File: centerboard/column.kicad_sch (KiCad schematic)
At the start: 5 parts

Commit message: centerboard messing around
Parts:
- added D1, D2, D3, D4: 1N4148W, Diode_SMD:D_SOD-123, symbol Diode:1N4148W
- added JC_LA: Conn_01x05_MountingPin, Connector_FFC-FPC:TE_84952-5_1x05-1MP_P1.0mm_Horizontal, symbol Connector_Generic_MountingPin:Conn_01x05_MountingPin
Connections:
- net COL: now also JC_LA.3 (Pin_3), JC_LA.3 (Pin_3); no longer JC_LA.5 (Pin_5)
- net at D3.2 (A): now also JC_LA.4 (Pin_4); no longer JC_LA.3 (Pin_3)
- net at D4.2 (A): now also JC_LA.5 (Pin_5); no longer JC_LA.4 (Pin_4)
- net ROW_1 renamed ROW_L4
- net ROW_2 renamed ROW_L3
- net ROW_3 renamed ROW_L2
- net ROW_4 renamed ROW_L1
- new net: D1.2 (A), JC_LA.1 (Pin_1)
- new net: D3.2 (A), JC_LA.4 (Pin_4)
- new net: D2.2 (A), JC_LA.2 (Pin_2)
- new net: D4.2 (A), JC_LA.5 (Pin_5)
- new net ROW_R1: D4.1 (K)
- new net ROW_R2: D3.1 (K)
- new net ROW_R3: D2.1 (K)
- new net ROW_R4: D1.1 (K)
- no-connect marks 0 -> 2

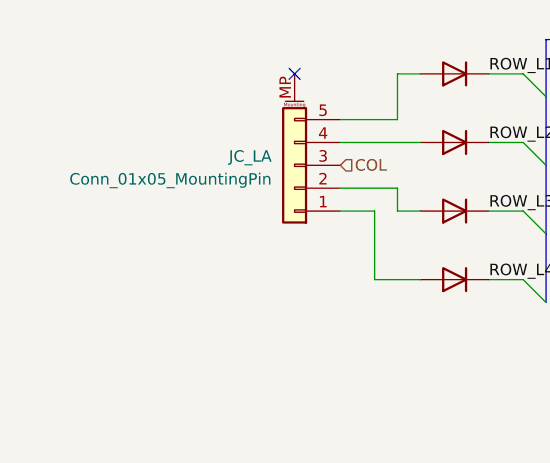
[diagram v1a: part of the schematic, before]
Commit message: Various tweaks. About to flip centerboard, not feeling too confident in the results there
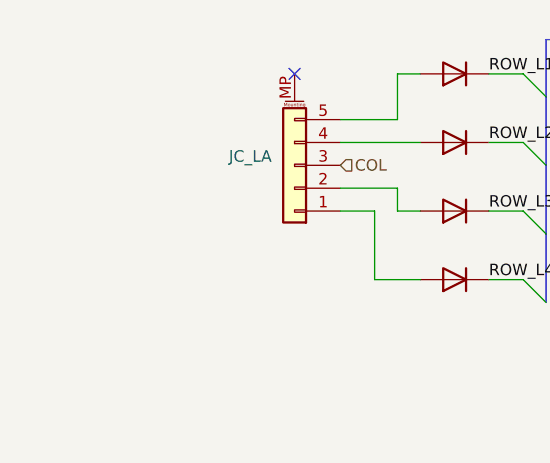
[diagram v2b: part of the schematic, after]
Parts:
- D1, D2, D3, D4: footprint Diode_SMD:D_SOD-123 -> Diode_SMD:D_0805_2012Metric
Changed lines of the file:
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@@
     )
     (property "Value" "Conn_01x05_MountingPin" (at 102.87 81.5594 0)
-      (effects (font (size 1.27 1.27)) (justify left))
+      (effects (font (size 1.27 1.27)) (justify left) hide)
     )
     (property "Footprint" "Connector_FFC-FPC:TE_84952-5_1x05-1MP_P1.0mm_Horizontal" (at 105.41 80.01 0)
@@
       (effects (font (size 1.27 1.27)) hide)
     )
-    (property "Footprint" "Diode_SMD:D_SOD-123" (at 207.01 111.125 0)
+    (property "Footprint" "Diode_SMD:D_0805_2012Metric" (at 207.01 111.125 0)
       (effects (font (size 1.27 1.27)) hide)
     )
@@
       (effects (font (size 1.27 1.27)) hide)
     )
-    (property "Footprint" "Diode_SMD:D_SOD-123" (at 123.19 88.265 0)
+    (property "Footprint" "Diode_SMD:D_0805_2012Metric" (at 123.19 88.265 0)
       (effects (font (size 1.27 1.27)) hide)
     )
@@
       (effects (font (size 1.27 1.27)) hide)
     )
-    (property "Footprint" "Diode_SMD:D_SOD-123" (at 207.01 95.885 0)
+    (property "Footprint" "Diode_SMD:D_0805_2012Metric" (at 207.01 95.885 0)
       (effects (font (size 1.27 1.27)) hide)
     )
@@
       (effects (font (size 1.27 1.27)) hide)
     )
-    (property "Footprint" "Diode_SMD:D_SOD-123" (at 123.19 65.405 0)
+    (property "Footprint" "Diode_SMD:D_0805_2012Metric" (at 123.19 65.405 0)
       (effects (font (size 1.27 1.27)) hide)
     )
@@
       (effects (font (size 1.27 1.27)) hide)
     )
-    (property "Footprint" "Diode_SMD:D_SOD-123" (at 123.19 73.025 0)
+    (property "Footprint" "Diode_SMD:D_0805_2012Metric" (at 123.19 73.025 0)
       (effects (font (size 1.27 1.27)) hide)
     )
@@
       (effects (font (size 1.27 1.27)) hide)
     )
-    (property "Footprint" "Diode_SMD:D_SOD-123" (at 207.01 103.505 0)
+    (property "Footprint" "Diode_SMD:D_0805_2012Metric" (at 207.01 103.505 0)
       (effects (font (size 1.27 1.27)) hide)
     )
@@
       (effects (font (size 1.27 1.27)) hide)
     )
-    (property "Footprint" "Diode_SMD:D_SOD-123" (at 123.19 80.645 0)
+    (property "Footprint" "Diode_SMD:D_0805_2012Metric" (at 123.19 80.645 0)
       (effects (font (size 1.27 1.27)) hide)
     )
@@
       (effects (font (size 1.27 1.27)) hide)
     )
-    (property "Footprint" "Diode_SMD:D_SOD-123" (at 207.01 88.265 0)
-      (effects (font (size 1.27 1.27)) hide)
-    )
+    (property "Footprint" "Diode_SMD:D_0805_2012Metric" (at 207.01 88.265 0)
+      (effects (font (size 1.27 1.27)) hide)
+    )

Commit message: centerboard redone, in 1.0 form I think
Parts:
- JC_LA: footprint Connector_FFC-FPC:TE_84952-5_1x05-1MP_P1.0mm_Horizontal -> panelization:FFC clamp fit 1x05 1.00mm; symbol Connector_Generic_MountingPin:Conn_01x05_MountingPin -> Connector_Generic:Conn_01x05
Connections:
- no-connect marks 2 -> 0
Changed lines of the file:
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@@
 (kicad_sch (version 20230121) (generator eeschema)
   (paper "A4")
-  (no_connect (at 189.23 92.71))
-  (no_connect (at 105.41 69.85))
   (bus_entry (at 214.63 107.95) (size 2.54 2.54)
     (stroke (width 0) (type default))
@@
     (effects (font (size 1.27 1.27)) (justify left))
   )
-  (symbol (lib_id "Connector_Generic_MountingPin:Conn_01x05_MountingPin") (at 105.41 80.01 180) (unit 1)
+  (symbol (lib_id "Connector_Generic:Conn_01x05") (at 105.41 80.01 180) (unit 1)
     (in_bom yes) (on_board yes) (dnp no) (fields_autoplaced)
     (property "Reference" "JC_LA" (at 102.87 79.0194 0)
@@
       (effects (font (size 1.27 1.27)) (justify left) hide)
     )
-    (property "Footprint" "Connector_FFC-FPC:TE_84952-5_1x05-1MP_P1.0mm_Horizontal" (at 105.41 80.01 0)
+    (property "Footprint" "panelization:FFC clamp fit 1x05 1.00mm" (at 105.41 80.01 0)
       (effects (font (size 1.27 1.27)) hide)
     )
@@
     (pin "4")
     (pin "5")
-    (pin "MP")
     (instances
       (project "centerboard"
@@
     )
   )
-  (symbol (lib_id "Connector_Generic_MountingPin:Conn_01x05_MountingPin") (at 189.23 102.87 180) (unit 1)
+  (symbol (lib_id "Connector_Generic:Conn_01x05") (at 189.23 102.87 180) (unit 1)
     (in_bom yes) (on_board yes) (dnp no) (fields_autoplaced)
     (property "Reference" "JC_LA" (at 186.69 101.8794 0)
@@
       (effects (font (size 1.27 1.27)) (justify left))
     )
-    (property "Footprint" "Connector_FFC-FPC:TE_84952-5_1x05-1MP_P1.0mm_Horizontal" (at 189.23 102.87 0)
+    (property "Footprint" "panelization:FFC clamp fit 1x05 1.00mm" (at 189.23 102.87 0)
       (effects (font (size 1.27 1.27)) hide)
     )
@@
     (pin "4")
     (pin "5")
-    (pin "MP")
-    (instances
-      (project "centerboard"
+    (instances
+      (project "centerboard"
